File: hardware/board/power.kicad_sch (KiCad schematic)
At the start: 21 parts, among them J2 Conn_01x02, Q1 AO3401A, U1 AMS1117-3.3, U9 TPS2113ADRBR

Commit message: v2 files
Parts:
- removed D5: ZMM5V6-M, Diode_SMD:D_MiniMELF, symbol Device:D_Zener
- removed Q1: AO3401A, Package_TO_SOT_SMD:SOT-23, symbol Transistor_FET:AO3401A
- removed R18: 680, Resistor_SMD:R_0603_1608Metric, symbol Device:R_Small
- added TP10 (x5), TP7, TP8, TP9 (x5): TestPoint, TestPoint:TestPoint_Pad_D1.5mm, symbol Connector:TestPoint
- D2: value EXT_PWR_IND -> KT-0603R; footprint LED_SMD:LED_0603_1608Metric -> ofc_sym:LED0603-RD
- D2: value USB_IND -> KT-0603R; footprint LED_SMD:LED_0603_1608Metric -> ofc_sym:LED0603-RD
- R22: footprint Resistor_SMD:R_0402_1005Metric -> Resistor_SMD:R_0603_1608Metric
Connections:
- net VIN is gone; now on net VIN_EXT: C24.1, R16.1, U9.6 (IN2)
- net +3V3: now also TP10.1, TP10.1, TP9.1, TP9.1
- net 5VIN: now also TP10.1
- net GND: now also TP10.1, TP10.1, TP9.1, TP9.1
- net PWR_STATE: now also TP9.1
- net VBUS: now also TP7.1
- net VIN_EXT: now also TP8.1
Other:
- note removed: "Reverse polarity protection for VIN_EXT"

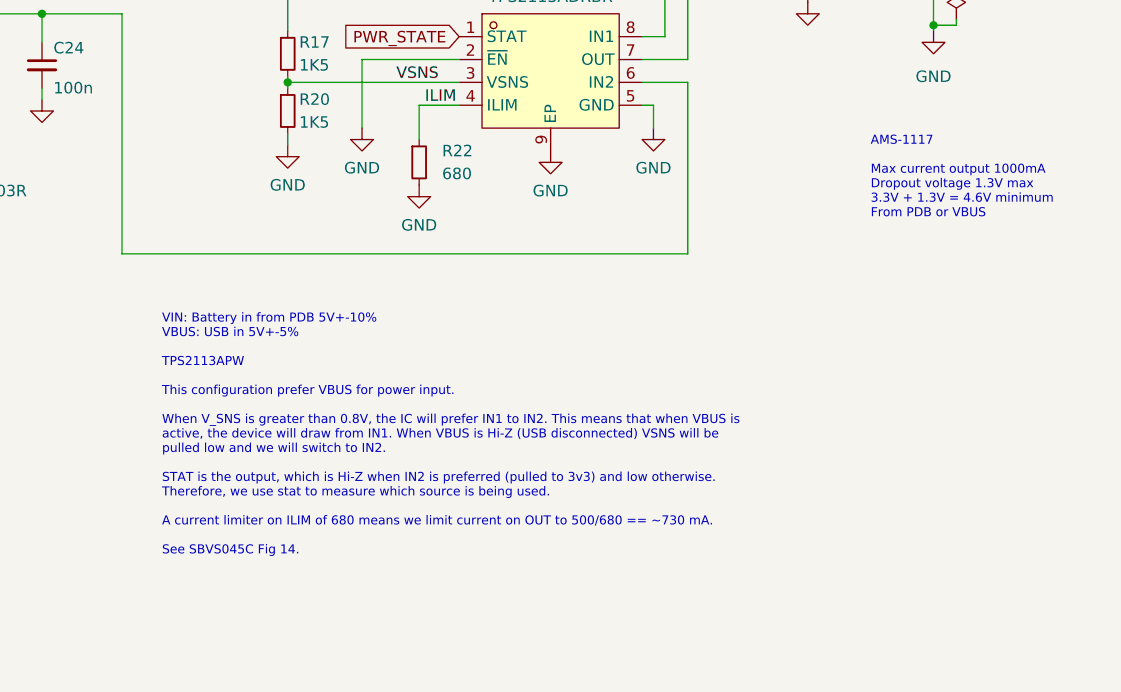
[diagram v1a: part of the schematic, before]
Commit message: Re-organize test points. Fix LED footprints #36
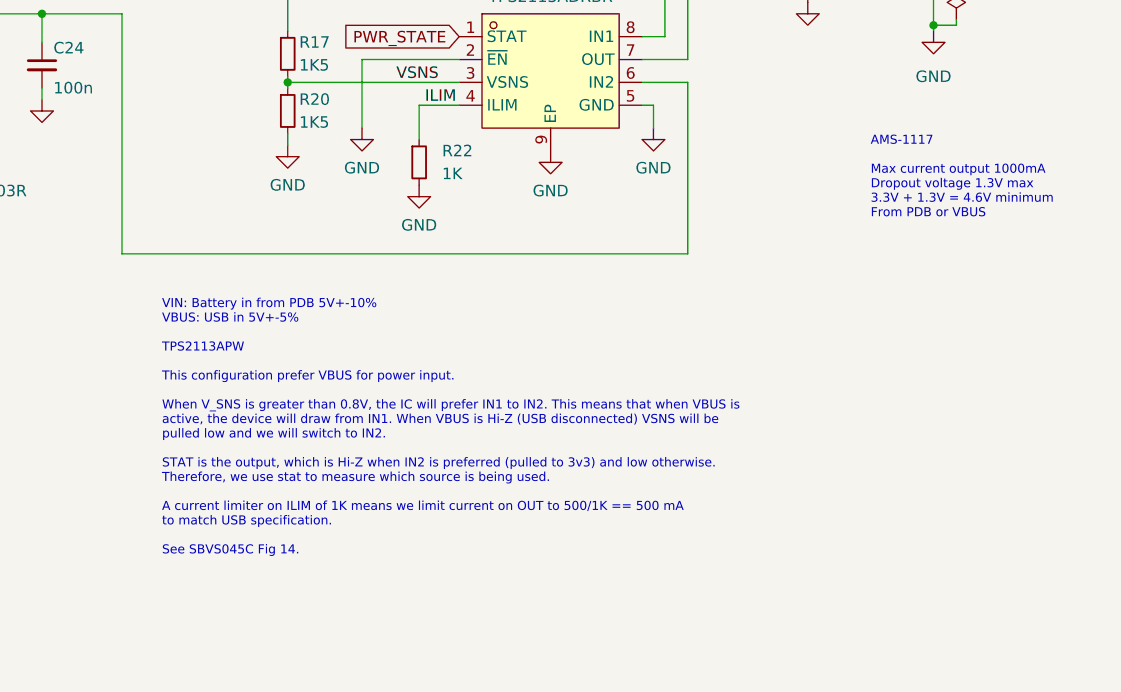
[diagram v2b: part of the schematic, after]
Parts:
- D2: footprint ofc_sym:LED0603-RD -> LED_SMD:LED_0603_1608Metric
- R22: value 680 -> 1K; footprint Resistor_SMD:R_0603_1608Metric -> Resistor_SMD:R_0402_1005Metric
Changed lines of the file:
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@@
     (effects (font (size 1 1)) (justify left bottom))
   )
-  (text "VIN: Battery in from PDB 5V+-10%\nVBUS: USB in 5V+-5%\n\nTPS2113APW\n\nThis configuration prefer VBUS for power input.\n\nWhen V_SNS is greater than 0.8V, the IC will prefer IN1 to IN2. This means that when VBUS is\nactive, the device will draw from IN1. When VBUS is Hi-Z (USB disconnected) VSNS will be\npulled low and we will switch to IN2. \n\nSTAT is the output, which is Hi-Z when IN2 is preferred (pulled to 3v3) and low otherwise. \nTherefore, we use stat to measure which source is being used.\n\nA current limiter on ILIM of 680 means we limit current on OUT to 500/680 == ~730 mA.\n\nSee SBVS045C Fig 14."
+  (text "VIN: Battery in from PDB 5V+-10%\nVBUS: USB in 5V+-5%\n\nTPS2113APW\n\nThis configuration prefer VBUS for power input.\n\nWhen V_SNS is greater than 0.8V, the IC will prefer IN1 to IN2. This means that when VBUS is\nactive, the device will draw from IN1. When VBUS is Hi-Z (USB disconnected) VSNS will be\npulled low and we will switch to IN2. \n\nSTAT is the output, which is Hi-Z when IN2 is preferred (pulled to 3v3) and low otherwise. \nTherefore, we use stat to measure which source is being used.\n\nA current limiter on ILIM of 1K means we limit current on OUT to 500/1K == 500 mA \nto match USB specification.\n\nSee SBVS045C Fig 14."
     (at 97.155 95.25 0)
     (effects (font (size 1 1)) (justify left bottom))
@@
       (effects (font (size 1.27 1.27)) (justify right))
     )
-    (property "Footprint" "ofc_sym:LED0603-RD" (at 72.39 53.34 90)
+    (property "Footprint" "LED_SMD:LED_0603_1608Metric" (at 72.39 53.34 90)
       (effects (font (size 1.27 1.27)) hide)
     )
@@
       (effects (font (size 1.27 1.27)) (justify left))
     )
-    (property "Value" "680" (at 128.27 52.705 0)
-      (effects (font (size 1.27 1.27)) (justify left))
-    )
-    (property "Footprint" "Resistor_SMD:R_0603_1608Metric" (at 125.73 51.435 0)
+    (property "Value" "1K" (at 128.27 52.705 0)
+      (effects (font (size 1.27 1.27)) (justify left))
+    )
+    (property "Footprint" "Resistor_SMD:R_0402_1005Metric" (at 125.73 51.435 0)
       (effects (font (size 1.27 1.27)) hide)
     )
@@
       (effects (font (size 1.27 1.27)) (justify right))
     )
-    (property "Footprint" "ofc_sym:LED0603-RD" (at 103.505 27.94 90)
-      (effects (font (size 1.27 1.27)) hide)
-    )
+    (property "Footprint" "LED_SMD:LED_0603_1608Metric" (at 103.505 27.94 90)
+      (effects (font (size 1.27 1.27)) hide)
+    )

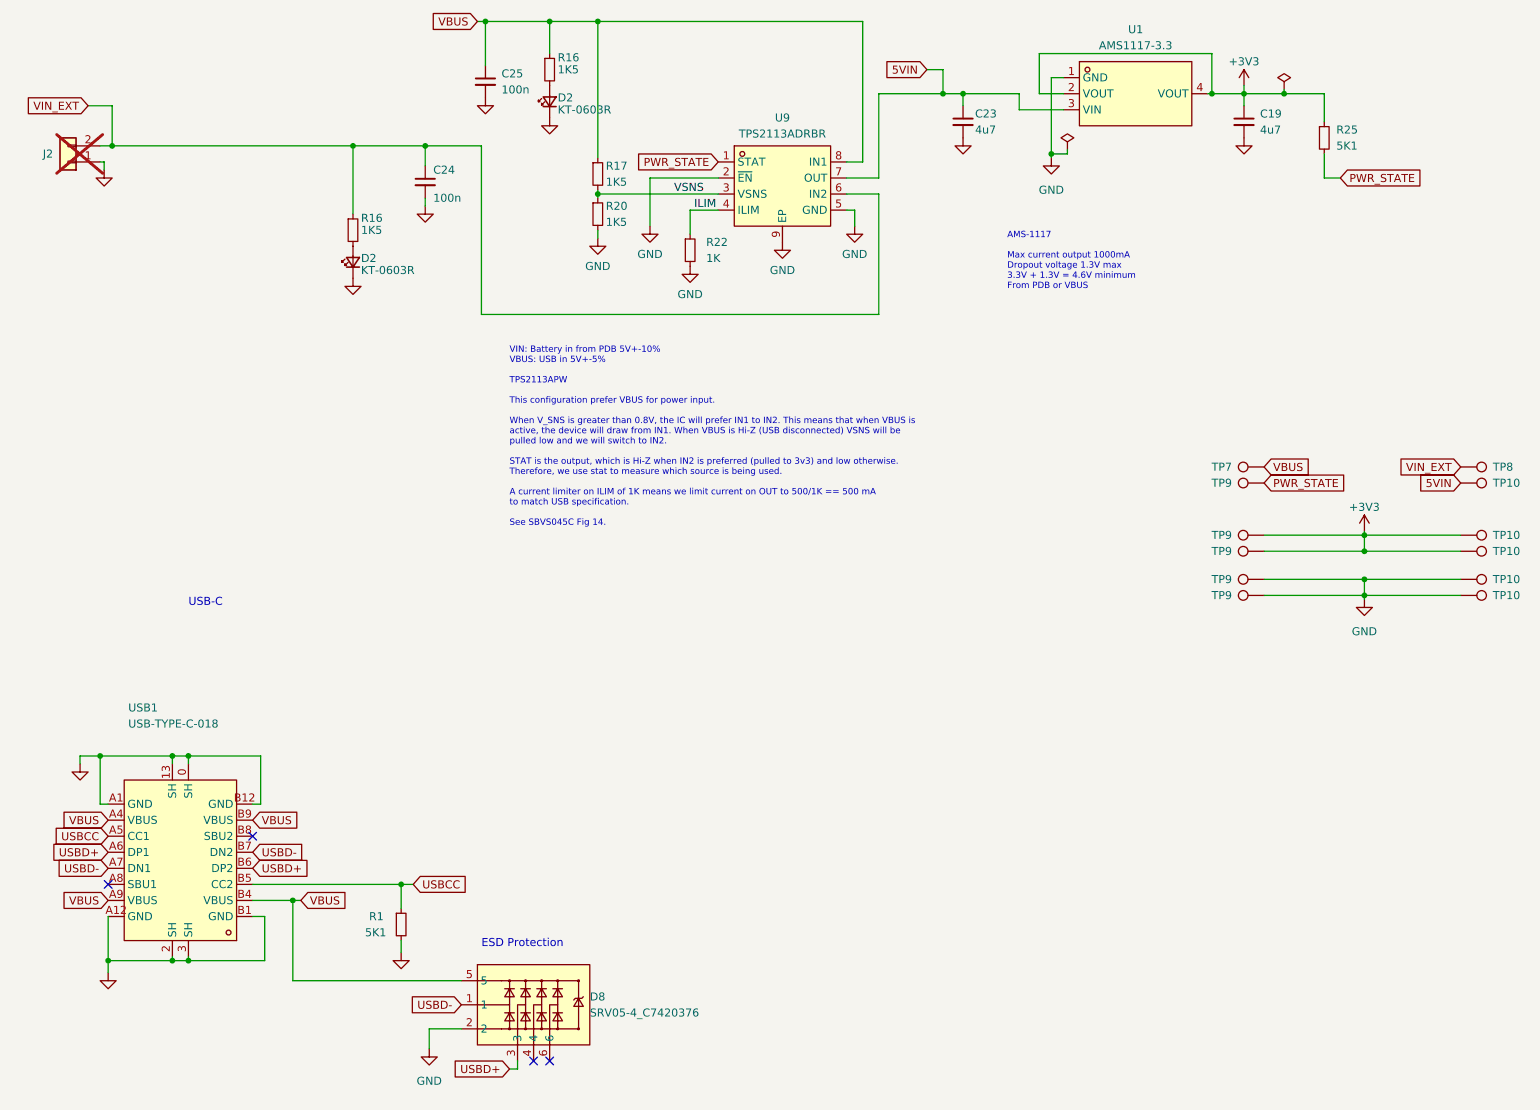
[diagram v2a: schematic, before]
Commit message: Added some organization to schematic
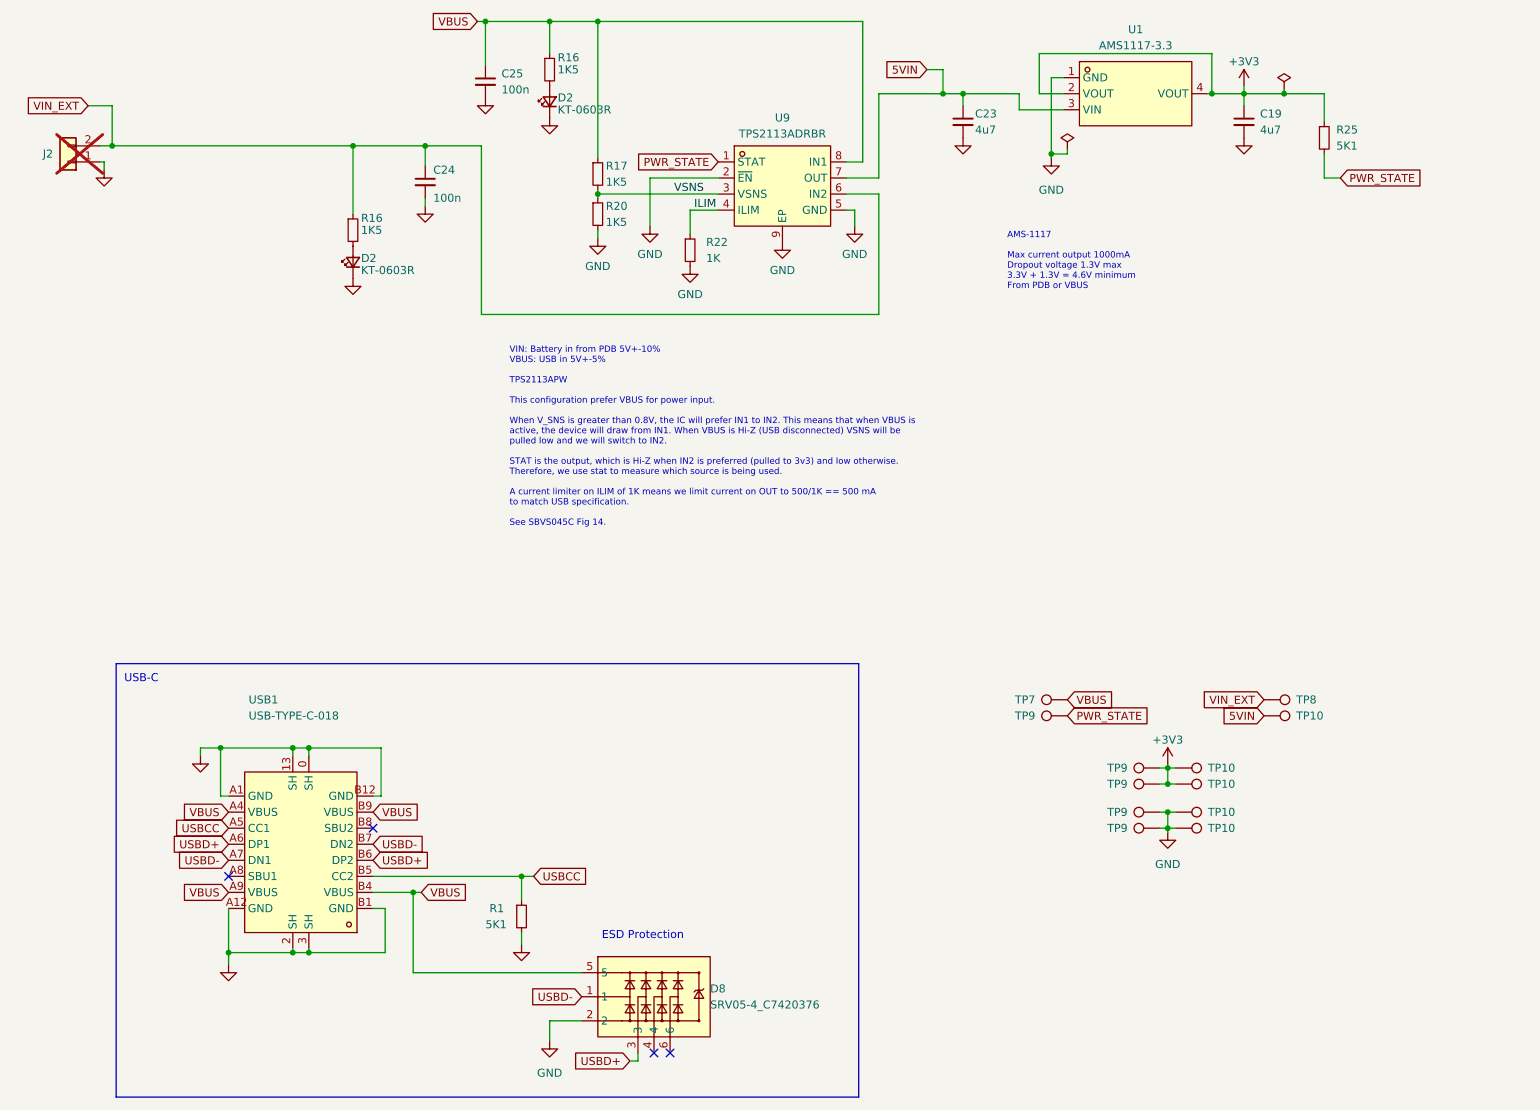
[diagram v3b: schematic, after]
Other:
- moved on the sheet: D8, R1, TP10, TP7, TP8, TP9, USB1
